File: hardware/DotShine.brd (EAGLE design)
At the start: 30 x 65 mm, 55 parts, among them CN1 1X4-BIG, IC1 CAT24M010TS, IC3 SI1145, J3 USB-MICROB, U1 ATMEGA328P-MU-QFN32, U2 TMP102, U3 ATSHA204-TSU, X2 MC-RTC-RV-4162-C7-I2C, X3 S4B-ZR

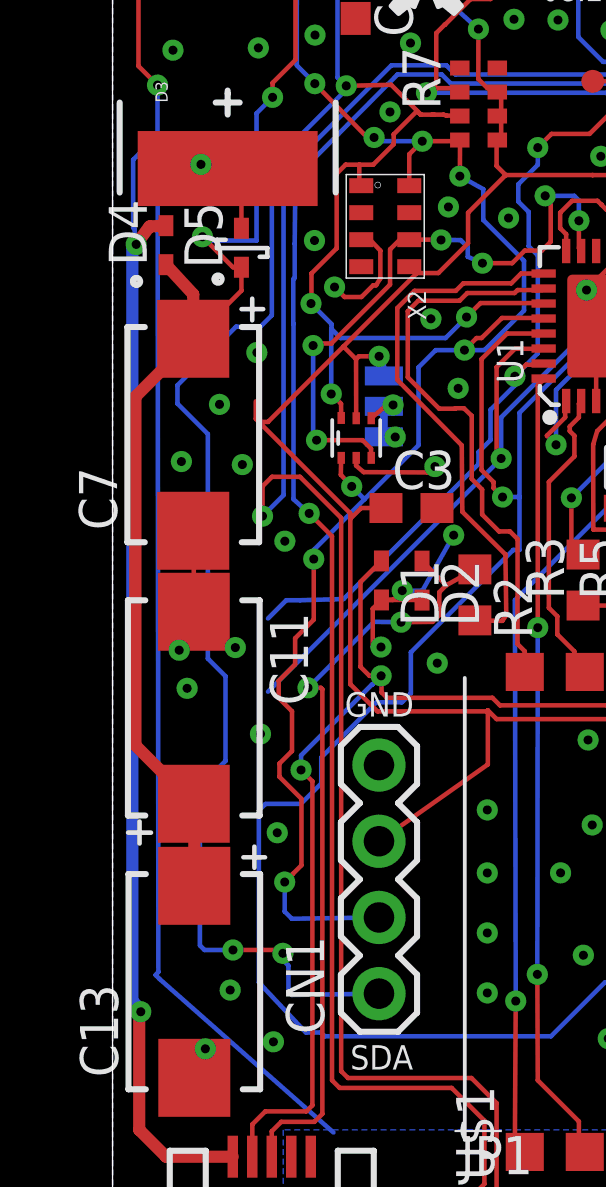
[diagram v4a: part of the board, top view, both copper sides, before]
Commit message: Move leftmost schottky left, overlap with stencil
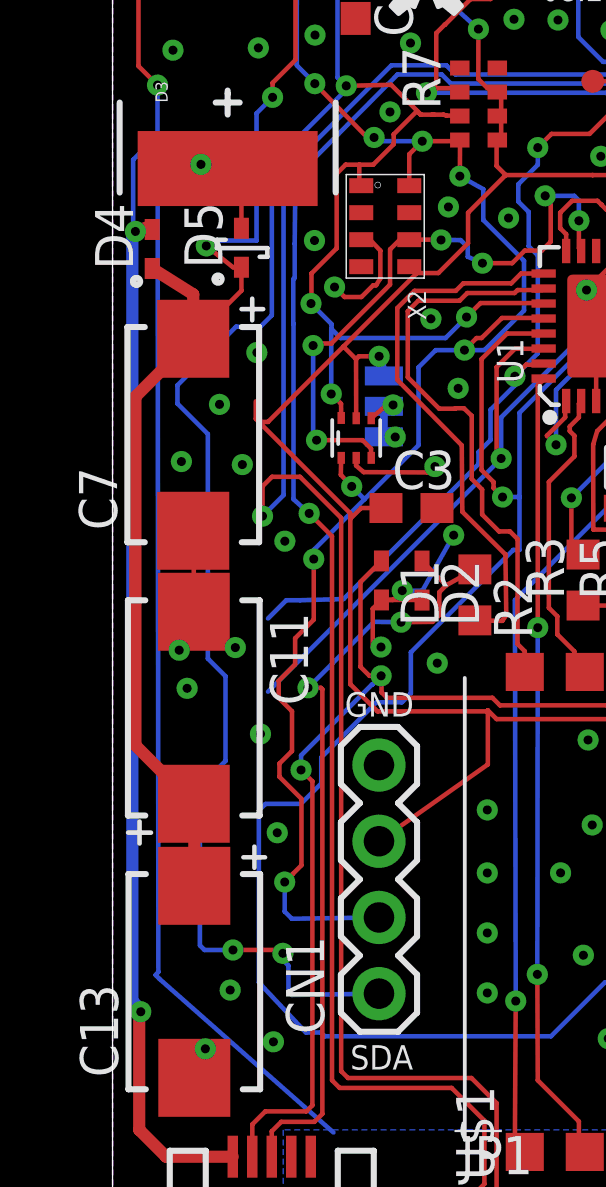
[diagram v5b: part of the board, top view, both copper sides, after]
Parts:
- moved D4 0.47 mm to (1.32, 34.5)
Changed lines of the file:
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@@
 <element name="D6" library="diode" package="SOD523" value="0.3V Schottky" x="12.232" y="47.296" rot="R90"/>
 <element name="J1" library="solderjumper" package="2.MED" value="" x="13.485" y="47.315" rot="R270"/>
-<element name="D4" library="diode" package="SOD523" value="0.3V Schottky" x="1.778" y="34.6456" rot="R90"/>
+<element name="D4" library="diode" package="SOD523" value="0.3V Schottky" x="1.3208" y="34.5186" rot="R90"/>
 </elements>
 <signals>
@@
 <wire x1="4.296" y1="33.181" x2="2.69" y2="31.575" width="0.1524" layer="1"/>
 <contactref element="D4" pad="C"/>
-<wire x1="1.778" y1="34.0456" x2="2.69" y2="33.0574" width="0.4064" layer="1"/>
+<wire x1="1.3208" y1="33.9186" x2="2.69" y2="33.0574" width="0.4064" layer="1"/>
 <wire x1="2.69" y1="33.0574" x2="2.69" y2="31.575" width="0.4064" layer="1"/>
 <wire x1="2.725" y1="16.058" x2="2.725" y2="13.34" width="0.4064" layer="1"/>
@@
 <wire x1="5.5626" y1="51.2826" x2="7.8774" y2="51.2826" width="0.1524" layer="1"/>
 <wire x1="7.8774" y1="51.2826" x2="8.14" y2="51.02" width="0.1524" layer="1"/>
-<via x="2.9972" y="34.9758" extent="1-16" drill="0.3"/>
+<via x="3.1242" y="34.671" extent="1-16" drill="0.3"/>
 <wire x1="4.8006" y1="34.8488" x2="4.8006" y2="39.0906" width="0.1524" layer="16"/>
 <wire x1="4.8006" y1="39.0906" x2="5.334" y2="39.624" width="0.1524" layer="16"/>
@@
 <wire x1="6.096" y1="50.7492" x2="5.5626" y2="51.2826" width="0.1524" layer="1"/>
 <wire x1="4.8006" y1="34.8488" x2="3.1242" y2="34.8488" width="0.1524" layer="16"/>
-<wire x1="3.1242" y1="34.8488" x2="2.9972" y2="34.9758" width="0.1524" layer="16"/>
+<wire x1="3.1242" y1="34.8488" x2="3.1242" y2="34.671" width="0.1524" layer="16"/>
 <wire x1="4.296" y1="33.96" x2="4.013" y2="33.96" width="0.1524" layer="1"/>
-<wire x1="4.013" y1="33.96" x2="2.9972" y2="34.9758" width="0.1524" layer="1"/>
+<wire x1="4.013" y1="33.96" x2="3.1242" y2="34.671" width="0.1524" layer="1"/>
 </signal>
 <signal name="N$7">
@@
 <wire x1="0.9398" y1="9.144" x2="0.9398" y2="9.2202" width="0.4064" layer="16"/>
 <wire x1="0.9398" y1="9.2202" x2="0.6604" y2="9.4996" width="0.4064" layer="16"/>
-<wire x1="0.6604" y1="9.4996" x2="0.6604" y2="34.6964" width="0.4064" layer="16"/>
-<wire x1="0.6604" y1="34.6964" x2="0.7874" y2="34.7218" width="0.4064" layer="16"/>
-<via x="0.7874" y="34.7218" extent="1-16" drill="0.3"/>
-<wire x1="0.7874" y1="34.7218" x2="1.2334" y2="35.3202" width="0.4064" layer="1"/>
-<wire x1="1.2334" y1="35.3202" x2="1.778" y2="35.3456" width="0.4064" layer="1"/>
+<wire x1="0.6604" y1="9.4996" x2="0.6604" y2="35.0012" width="0.4064" layer="16"/>
+<wire x1="0.6604" y1="35.0012" x2="0.762" y2="35.1536" width="0.4064" layer="16"/>
+<via x="0.762" y="35.1536" extent="1-16" drill="0.3"/>
+<wire x1="0.762" y1="35.1536" x2="1.2334" y2="35.3202" width="0.4064" layer="1"/>
+<wire x1="1.2334" y1="35.3202" x2="1.3208" y2="35.2186" width="0.4064" layer="1"/>
 <contactref element="LED2" pad="A"/>
 <wire x1="8.343165625" y1="60.967659375" x2="8.343165625" y2="58.355765625" width="0.1524" layer="1"/>
@@
 <wire x1="0.6858" y1="35.2806" x2="0.7366" y2="35.2298" width="0.1524" layer="16"/>
 <wire x1="0.7366" y1="35.2298" x2="0.7366" y2="34.7726" width="0.1524" layer="16"/>
-<wire x1="0.7366" y1="34.7726" x2="0.7874" y2="34.7218" width="0.1524" layer="16"/>
+<wire x1="0.7366" y1="34.7726" x2="0.762" y2="35.1536" width="0.1524" layer="16"/>
 </signal>
 </signals>

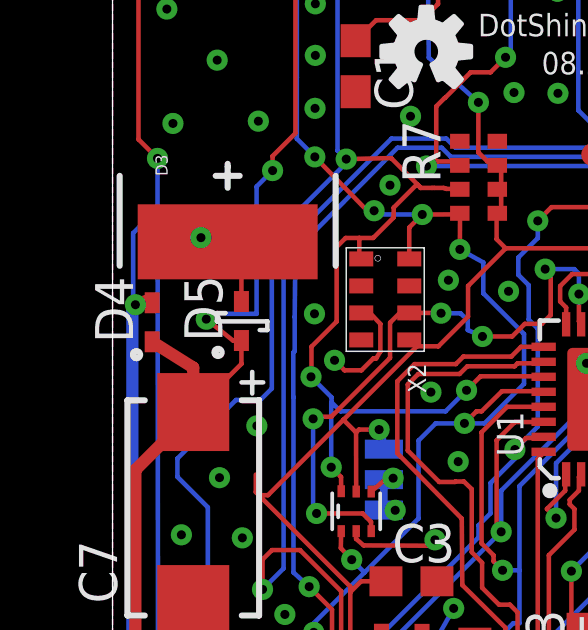
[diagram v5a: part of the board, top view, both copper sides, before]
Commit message: Realign leftmost schottky
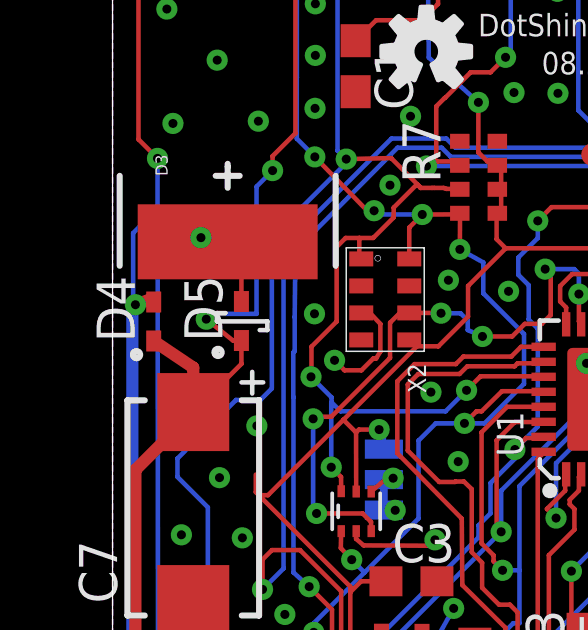
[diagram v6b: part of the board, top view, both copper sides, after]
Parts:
- moved D4 0.06 mm to (1.37, 34.5)
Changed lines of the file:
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@@
 <element name="D6" library="diode" package="SOD523" value="0.3V Schottky" x="12.232" y="47.296" rot="R90"/>
 <element name="J1" library="solderjumper" package="2.MED" value="" x="13.485" y="47.315" rot="R270"/>
-<element name="D4" library="diode" package="SOD523" value="0.3V Schottky" x="1.3208" y="34.5186" rot="R90"/>
+<element name="D4" library="diode" package="SOD523" value="0.3V Schottky" x="1.3716" y="34.544" rot="R90"/>
 </elements>
 <signals>
@@
 <wire x1="4.296" y1="33.181" x2="2.69" y2="31.575" width="0.1524" layer="1"/>
 <contactref element="D4" pad="C"/>
-<wire x1="1.3208" y1="33.9186" x2="2.69" y2="33.0574" width="0.4064" layer="1"/>
+<wire x1="1.3716" y1="33.944" x2="2.69" y2="33.0574" width="0.4064" layer="1"/>
 <wire x1="2.69" y1="33.0574" x2="2.69" y2="31.575" width="0.4064" layer="1"/>
 <wire x1="2.725" y1="16.058" x2="2.725" y2="13.34" width="0.4064" layer="1"/>
@@
 <via x="0.762" y="35.1536" extent="1-16" drill="0.3"/>
 <wire x1="0.762" y1="35.1536" x2="1.2334" y2="35.3202" width="0.4064" layer="1"/>
-<wire x1="1.2334" y1="35.3202" x2="1.3208" y2="35.2186" width="0.4064" layer="1"/>
+<wire x1="1.2334" y1="35.3202" x2="1.3716" y2="35.244" width="0.4064" layer="1"/>
 <contactref element="LED2" pad="A"/>
 <wire x1="8.343165625" y1="60.967659375" x2="8.343165625" y2="58.355765625" width="0.1524" layer="1"/>
